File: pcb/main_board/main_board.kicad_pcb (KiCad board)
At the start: 2 copper layers, 120 x 54.8 mm, 0 parts

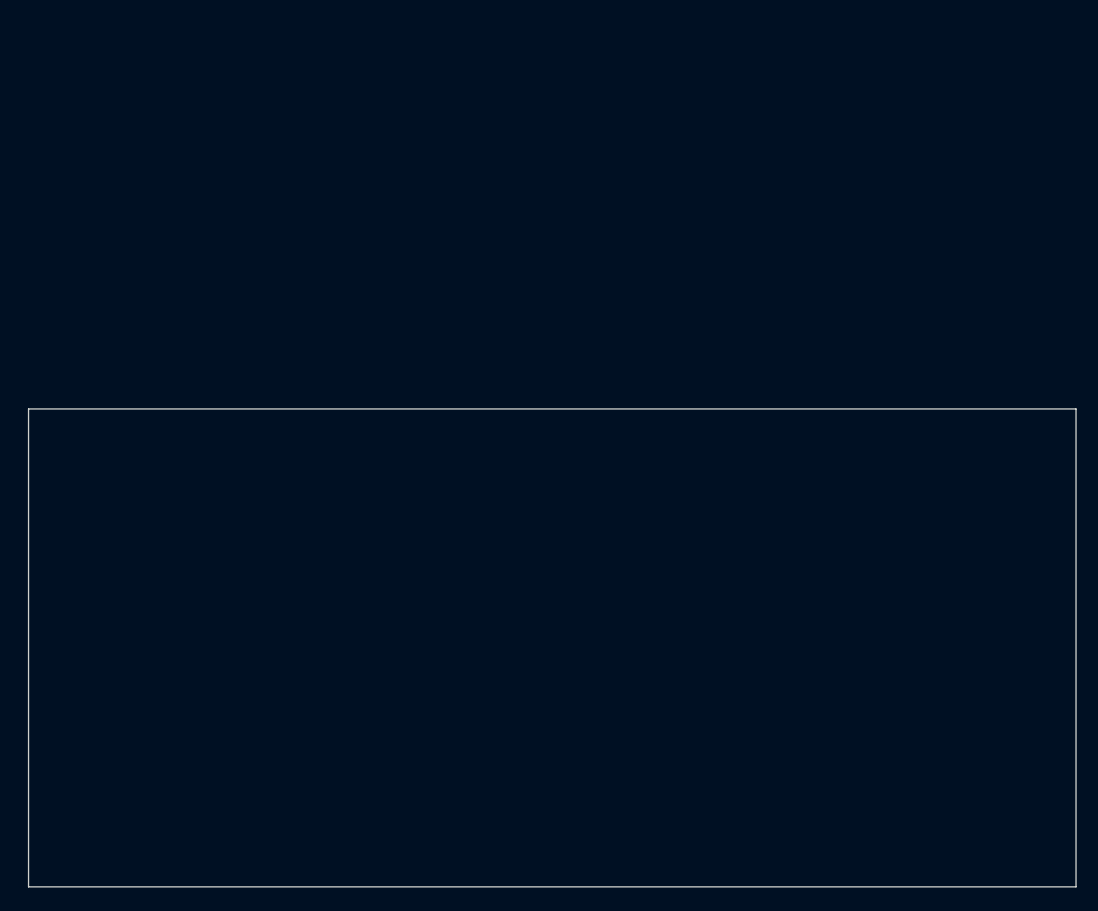
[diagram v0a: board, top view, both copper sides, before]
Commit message: Kicadification complete, not bothering to make the PCB though because it's about to get integrated onto the keyboard anyway
Signed-off-by: James Hughes <james@pyrosoftsolutions.co.uk>
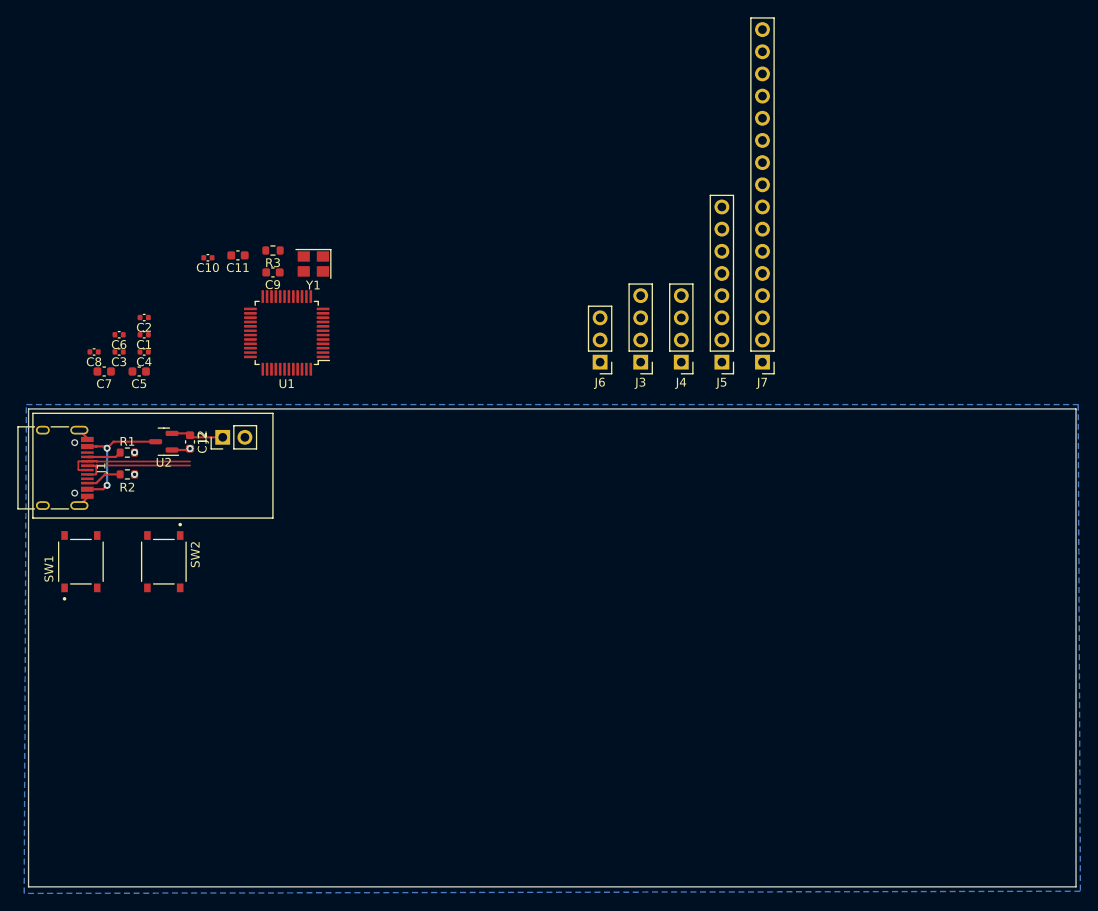
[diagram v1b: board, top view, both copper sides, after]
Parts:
- added C1: 12pF, Capacitor_SMD:C_0402_1005Metric, F.Cu at (91.8, 50.5)
- added C10: 100nF, Capacitor_SMD:C_0402_1005Metric, F.Cu at (99.0, 41.7)
- added C11: 4.7uF, Capacitor_SMD:C_0603_1608Metric, F.Cu at (102.5, 41.4)
- added C12: 1uF, Capacitor_SMD:C_0603_1608Metric, F.Cu at (97.0, 62.8)
- added C2: 12pF, Capacitor_SMD:C_0402_1005Metric, F.Cu at (91.8, 48.5)
- added C3: 100nF, Capacitor_SMD:C_0402_1005Metric, F.Cu at (88.9, 52.5)
- added C4: 100nF, Capacitor_SMD:C_0402_1005Metric, F.Cu at (91.8, 52.5)
- added C5: 4.7uF, Capacitor_SMD:C_0603_1608Metric, F.Cu at (91.2, 54.7)
- added C6: 100nF, Capacitor_SMD:C_0402_1005Metric, F.Cu at (88.9, 50.5)
- added C7: 4.7uF, Capacitor_SMD:C_0603_1608Metric, F.Cu at (87.2, 54.7)
- added C8: 10nf, Capacitor_SMD:C_0402_1005Metric, F.Cu at (86.0, 52.5)
- added C9: 1uF, Capacitor_SMD:C_0603_1608Metric, F.Cu at (106.5, 43.4)
- added J1: USB_C_Receptacle_USB2.0, Connector_USB:USB_C_Receptacle_HRO_TYPE-C-31-M-12, F.Cu at (81.2, 65.8)
- added J2: Conn_01x02_Female, Connector_PinHeader_2.54mm:PinHeader_1x02_P2.54mm_Vertical, F.Cu at (100.8, 62.2)
- added J3: Conn_01x04_Female, Connector_PinHeader_2.54mm:PinHeader_1x04_P2.54mm_Vertical, F.Cu at (148.6, 53.6)
- added J4: Conn_01x04_Female, Connector_PinHeader_2.54mm:PinHeader_1x04_P2.54mm_Vertical, F.Cu at (153.3, 53.6)
- added J5: Conn_01x08_Female, Connector_PinHeader_2.54mm:PinHeader_1x08_P2.54mm_Vertical, F.Cu at (157.9, 53.6)
- added J6: Conn_01x03_Female, Connector_PinHeader_2.54mm:PinHeader_1x03_P2.54mm_Vertical, F.Cu at (144.0, 53.6)
- added J7: Conn_01x16_Female, Connector_PinHeader_2.54mm:PinHeader_1x16_P2.54mm_Vertical, F.Cu at (162.6, 53.6)
- added R1: 5.1k, Resistor_SMD:R_0603_1608Metric, F.Cu at (89.8, 64.0)
- added R2: 5.1kR, Resistor_SMD:R_0603_1608Metric, F.Cu at (89.8, 66.5)
- added R3: 10kR, Resistor_SMD:R_0603_1608Metric, F.Cu at (106.5, 40.9)
- added SW1: SW_Push_Dual, ProjectLib:SW_TS-1187A-B-A-B, F.Cu at (84.5, 76.5)
- added SW2: SW_Push_Dual, ProjectLib:SW_TS-1187A-B-A-B, F.Cu at (94.0, 76.5)
- added U1: STM32F072C8Tx, Package_QFP:LQFP-48_7x7mm_P0.5mm, F.Cu at (108.1, 50.3)
- added U2: XC6206PxxxMR, Package_TO_SOT_SMD:SOT-23, F.Cu at (94.0, 62.8)
- added Y1: Crystal_GND24_Small, Crystal:Crystal_SMD_3225-4Pin_3.2x2.5mm, F.Cu at (111.1, 42.4)
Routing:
- net /USB_IN/D-: track 0.00 -> 15.8 mm
- net /USB_IN/VBUS: track 0.00 -> 15.0 mm, vias 0 -> 2
- net /USB_IN/D+: track 0.00 -> 14.8 mm
- net VCC: track 0.00 -> 6.00 mm
- net GND: track 0.00 -> 5.04 mm, vias 0 -> 3
- net Net-(J1-PadB5): track 0.00 -> 4.18 mm
- net Net-(J1-PadA5): track 0.00 -> 3.97 mm
- added copper zone on B.Cu, net GND
